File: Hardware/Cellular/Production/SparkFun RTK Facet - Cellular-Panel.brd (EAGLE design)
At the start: 140.6 x 186.3 mm, 776 parts, among them IC1 SN74AVC4T774PW, IC10 SN74AVC4T774PW, IC2 SN74AVC4T774PW, IC3 SN74AVC4T774PW, IC4 SN74AVC4T774PW, IC5 SN74AVC4T774PW, IC6 SN74AVC4T774PW, IC7 SN74AVC4T774PW, IC8 SN74AVC4T774PW, IC9 SN74AVC4T774PW, J10 U.FL, J13 DIAG, J14 U.FL, J17 DIAG, J18 U.FL, J2 U.FL, J21 DIAG, J22 U.FL, J25 DIAG, J26 U.FL, J29 DIAG, J3 DIAG, J30 U.FL, J33 DIAG, J34 U.FL, J37 DIAG, J38 U.FL, J5 DIAG, J6 U.FL, J9 DIAG, Q1 20V/0.2A/8MHz/1.2Ω/1Vth, Q10 310mA/60V/1.6Ω, Q11 310mA/60V/1.6Ω, Q12 20V/0.2A/8MHz/1.2Ω/1Vth, Q13 310mA/60V/1.6Ω, Q14 310mA/60V/1.6Ω, Q15 20V/0.2A/8MHz/1.2Ω/1Vth, Q16 310mA/60V/1.6Ω, Q17 310mA/60V/1.6Ω, Q18 20V/0.2A/8MHz/1.2Ω/1Vth, Q19 310mA/60V/1.6Ω, Q2 310mA/60V/1.6Ω, Q20 310mA/60V/1.6Ω, Q21 20V/0.2A/8MHz/1.2Ω/1Vth, Q22 310mA/60V/1.6Ω, Q23 310mA/60V/1.6Ω, Q24 20V/0.2A/8MHz/1.2Ω/1Vth, Q25 310mA/60V/1.6Ω, Q26 310mA/60V/1.6Ω, Q27 20V/0.2A/8MHz/1.2Ω/1Vth, Q28 310mA/60V/1.6Ω, Q29 310mA/60V/1.6Ω, Q3 310mA/60V/1.6Ω, Q30 20V/0.2A/8MHz/1.2Ω/1Vth, Q4 310mA/60V/1.6Ω, Q5 310mA/60V/1.6Ω, Q6 20V/0.2A/8MHz/1.2Ω/1Vth, Q7 310mA/60V/1.6Ω, Q8 310mA/60V/1.6Ω, Q9 20V/0.2A/8MHz/1.2Ω/1Vth, U1 SARA-R510M8S, U10 SARA-R510M8S, U11 74HC1G04, U12 AP2112K-3.3, U13 SARA-R510M8S, U14 74HC1G04, U15 AP2112K-3.3, U16 SARA-R510M8S, U17 74HC1G04, U18 AP2112K-3.3, U19 SARA-R510M8S, U2 74HC1G04, U20 74HC1G04, U21 AP2112K-3.3, U22 SARA-R510M8S, U23 74HC1G04, U24 AP2112K-3.3, U25 SARA-R510M8S, U26 74HC1G04, U27 AP2112K-3.3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

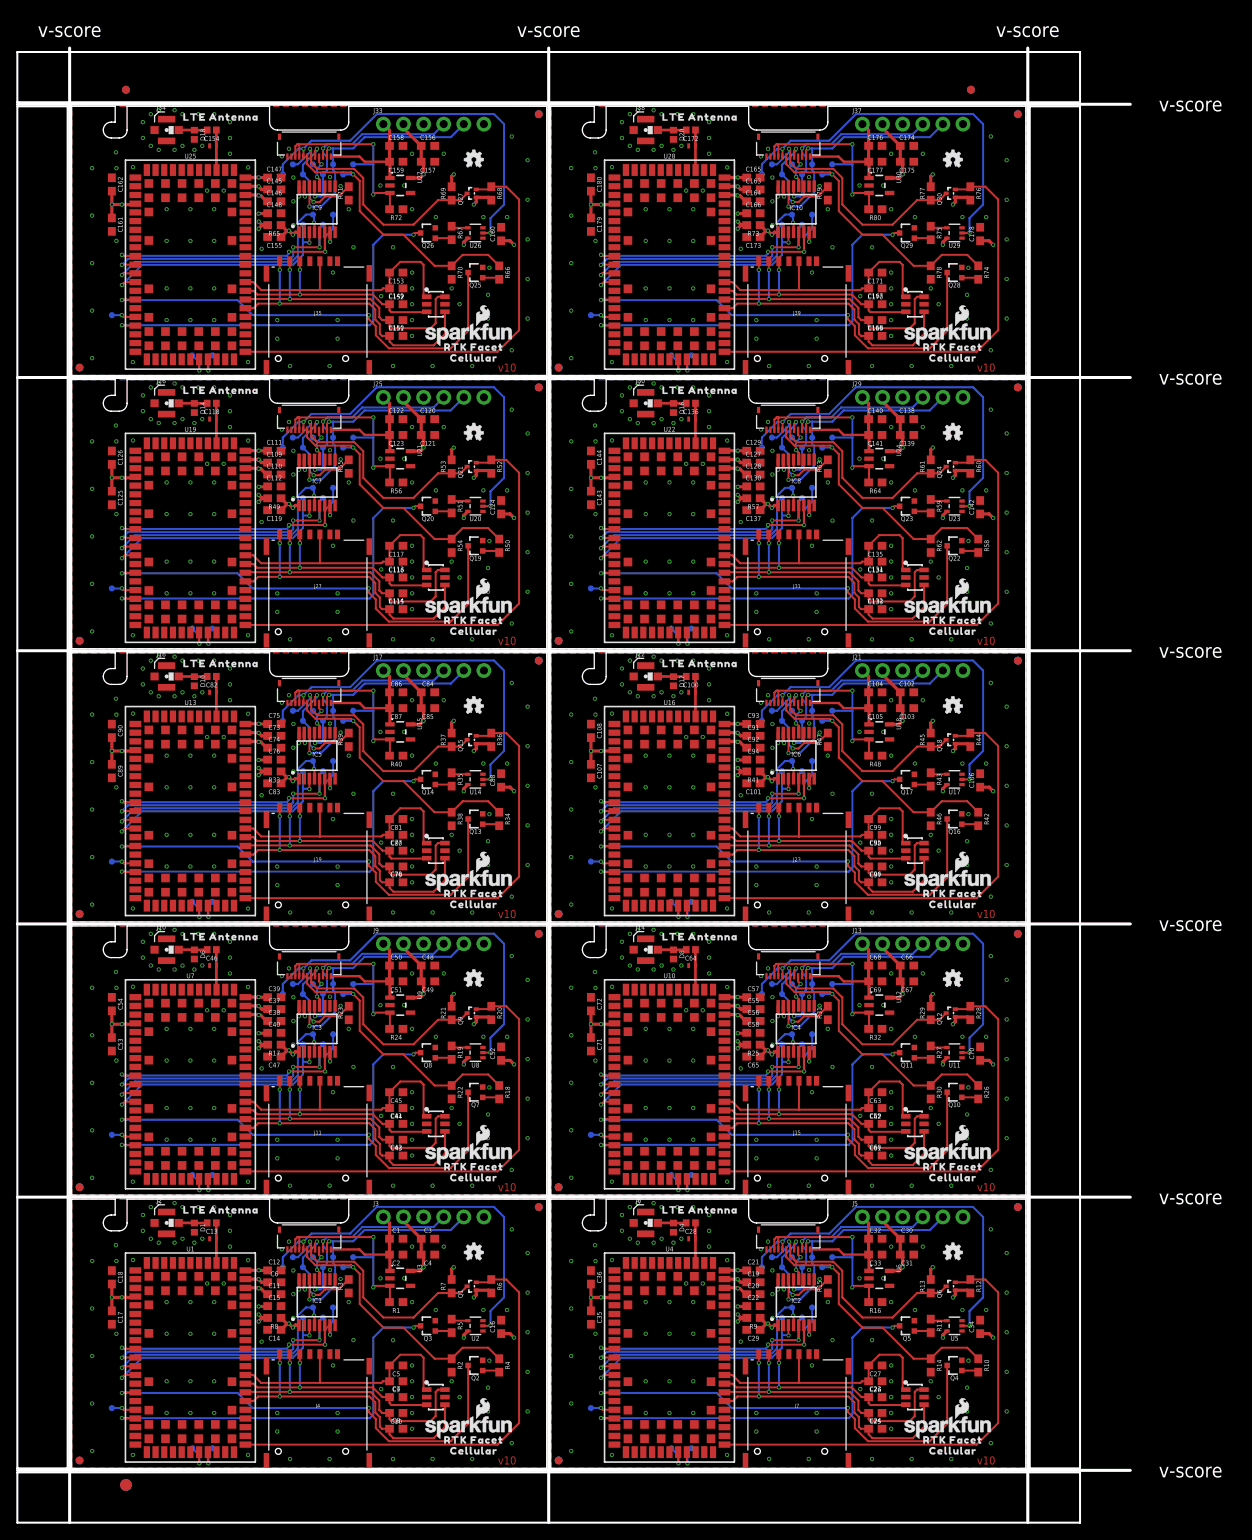
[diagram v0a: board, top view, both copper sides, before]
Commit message: Reduce Main, Connector, Display, and Cell board widths by 1mm to allow for v-score protrusion.
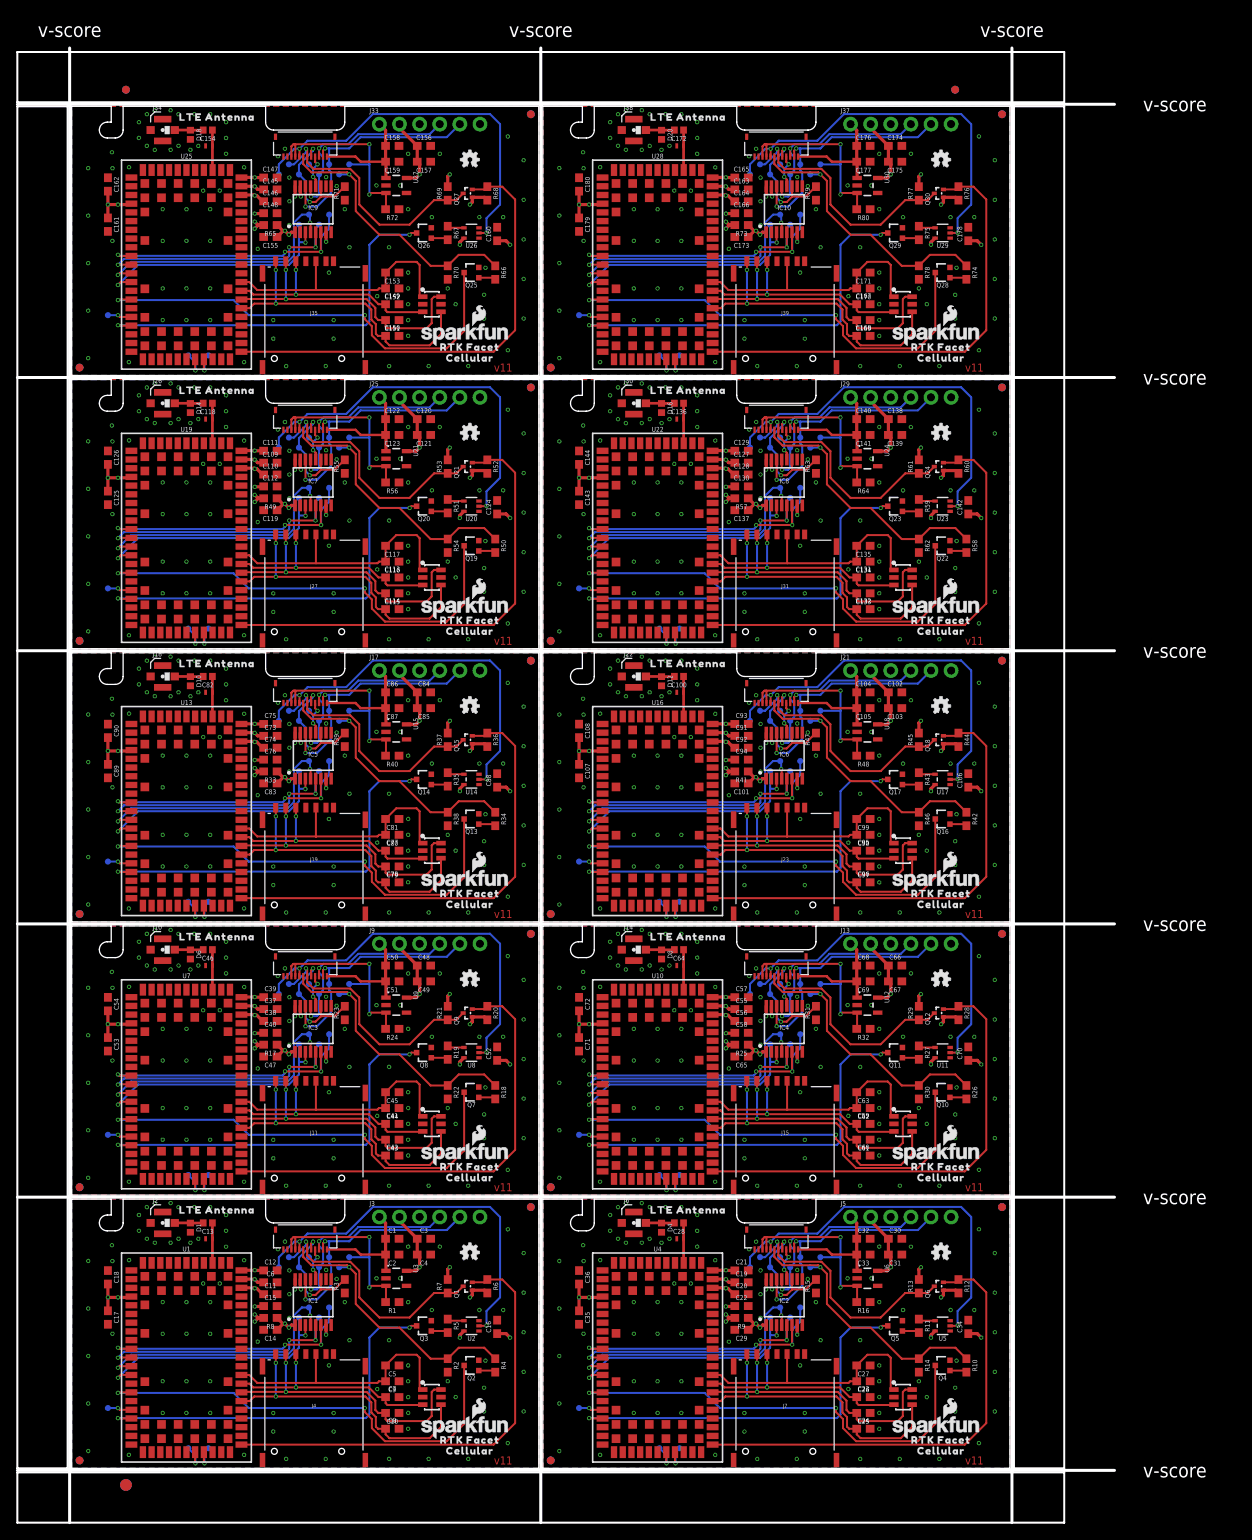
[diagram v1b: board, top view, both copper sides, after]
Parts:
- moved FID14 2.00 mm to (117.5, 67.5)
- moved FID15 2.00 mm to (117.5, 67.5)
- moved FID22 2.00 mm to (117.5, 102.0)
- moved FID23 2.00 mm to (117.5, 102.0)
- moved FID30 2.00 mm to (117.5, 136.5)
- moved FID31 2.00 mm to (117.5, 136.5)
- moved FID38 2.00 mm to (117.5, 171.0)
- moved FID39 2.00 mm to (117.5, 171.0)
- moved FID6 2.00 mm to (117.5, 33.0)
- moved FID7 2.00 mm to (117.5, 33.0)
- moved E$3 2.00 mm to (111.6, 174.1)
- moved E$4 2.00 mm to (111.6, 174.1)
- moved C101 1.50 mm to (84.6, 86.5)
- moved C106 1.50 mm to (113.2, 86.9)
- moved C127 1.50 mm to (84.6, 127.0)
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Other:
- board size 140.6 x 186.3 mm -> 138.6 x 186.3 mm
- board text added: "v11"
- board text removed: "v10"
